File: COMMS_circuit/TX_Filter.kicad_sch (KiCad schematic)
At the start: 6 parts

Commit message: testing opsec update
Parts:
- added R61: 1k, Resistor_SMD:R_0402_1005Metric, symbol Device:R
- renumbered C11 to C33, C26 to C34, C25 to C35, L4 to L13, L6 to L14, L5 to L15
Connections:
- net AGND: now also R61.2
- net at C34.2, C35.1, L13.2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: now also R61.1
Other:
- moved on the sheet: C35, L14, L15

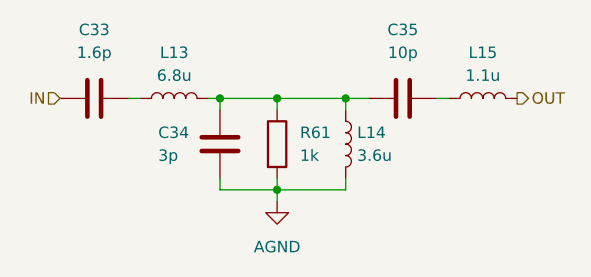
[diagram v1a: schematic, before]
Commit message: Stick a RP2040 on the side and see if we can program an FPGA with it
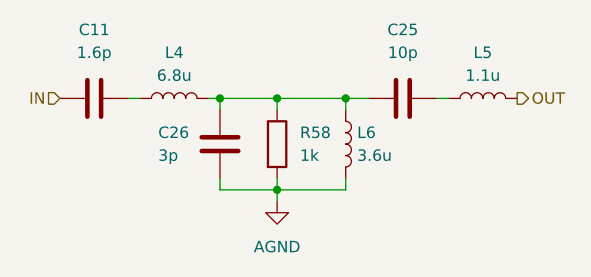
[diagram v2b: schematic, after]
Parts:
- renumbered C33 to C11, C35 to C25, C34 to C26, L13 to L4, L15 to L5, L14 to L6, R61 to R58
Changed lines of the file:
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@@
 (kicad_sch
-	(version 20231120)
+	(version 20250114)
 	(generator "eeschema")
-	(generator_version "8.0")
+	(generator_version "9.0")
 	(paper "A")
 	(junction
@@
 		(dnp no)
 		(fields_autoplaced yes)
-		(property "Reference" "L14"
+		(property "Reference" "L6"
 			(at 109.22 85.0899 0)
 			(effects
@@
 		(dnp no)
 		(fields_autoplaced yes)
-		(property "Reference" "L15"
+		(property "Reference" "L5"
 			(at 123.19 76.2 90)
 			(effects
@@
 		(dnp no)
 		(fields_autoplaced yes)
-		(property "Reference" "L13"
+		(property "Reference" "L4"
 			(at 88.9 76.2 90)
 			(effects
@@
 		(dnp no)
 		(fields_autoplaced yes)
-		(property "Reference" "C35"
+		(property "Reference" "C25"
 			(at 114.3 73.66 90)
 			(effects
@@
 		(dnp no)
 		(fields_autoplaced yes)
-		(property "Reference" "R61"
+		(property "Reference" "R58"
 			(at 102.87 85.0899 0)
 			(effects
@@
 		(dnp no)
 		(fields_autoplaced yes)
-		(property "Reference" "C33"
+		(property "Reference" "C11"
 			(at 80.01 73.66 90)
 			(effects
@@
 		(on_board yes)
 		(dnp no)
-		(property "Reference" "C34"
+		(property "Reference" "C26"
 			(at 87.122 85.09 0)
 			(effects
@@
 		(dnp no)
 		(fields_autoplaced yes)
-		(property "Reference" "#PWR030"
+		(property "Reference" "#PWR018"
 			(at 100.33 99.06 0)
 			(effects
